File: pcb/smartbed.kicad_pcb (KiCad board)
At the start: 2 copper layers, 59.5 x 51.5 mm, 51 parts, among them J1 USB_MICRO_A, J2 SBBUS_1, J3 DBGCON, J6 FSRCON1, J7 FSRCON2, J8 SBBUS_2, SW1 SW_SPST, U1 LD1117S33CTR, U2 ATSAMD21J18A, Y1 Crystal

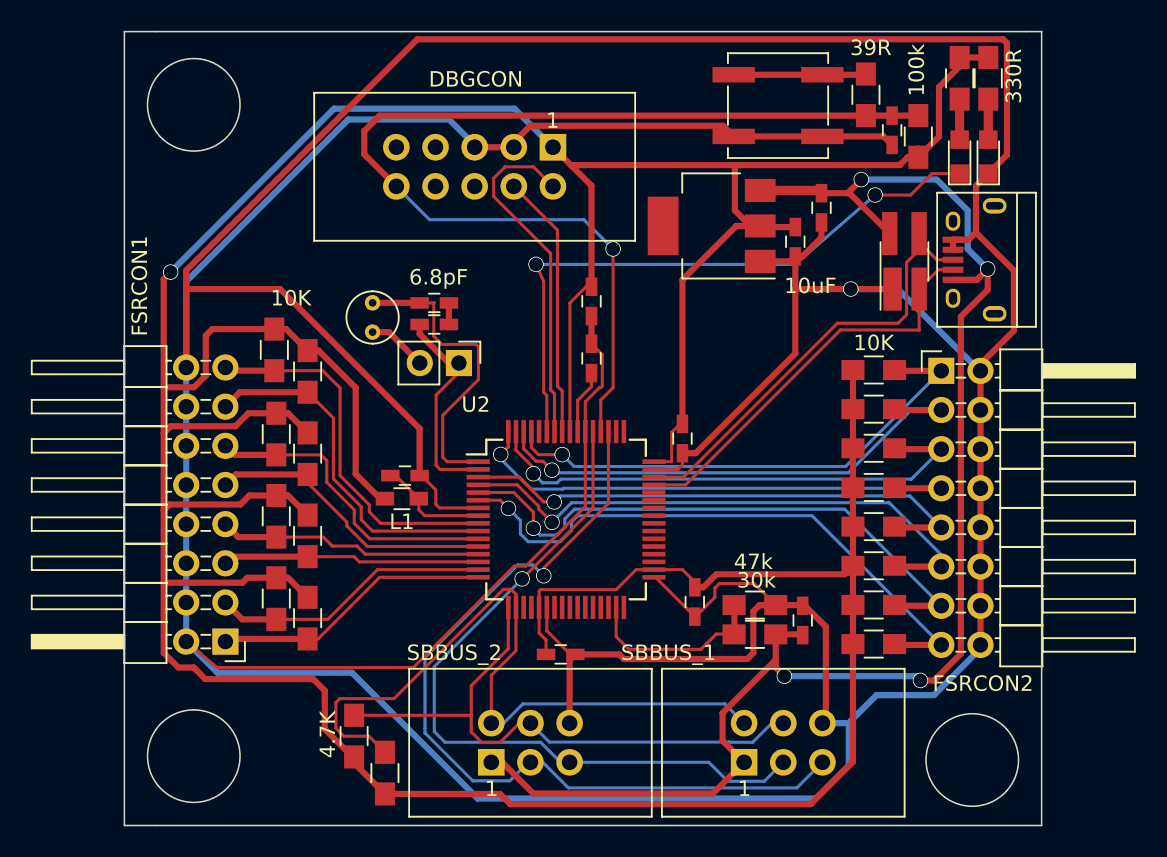
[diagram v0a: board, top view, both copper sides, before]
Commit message: Add ground planes
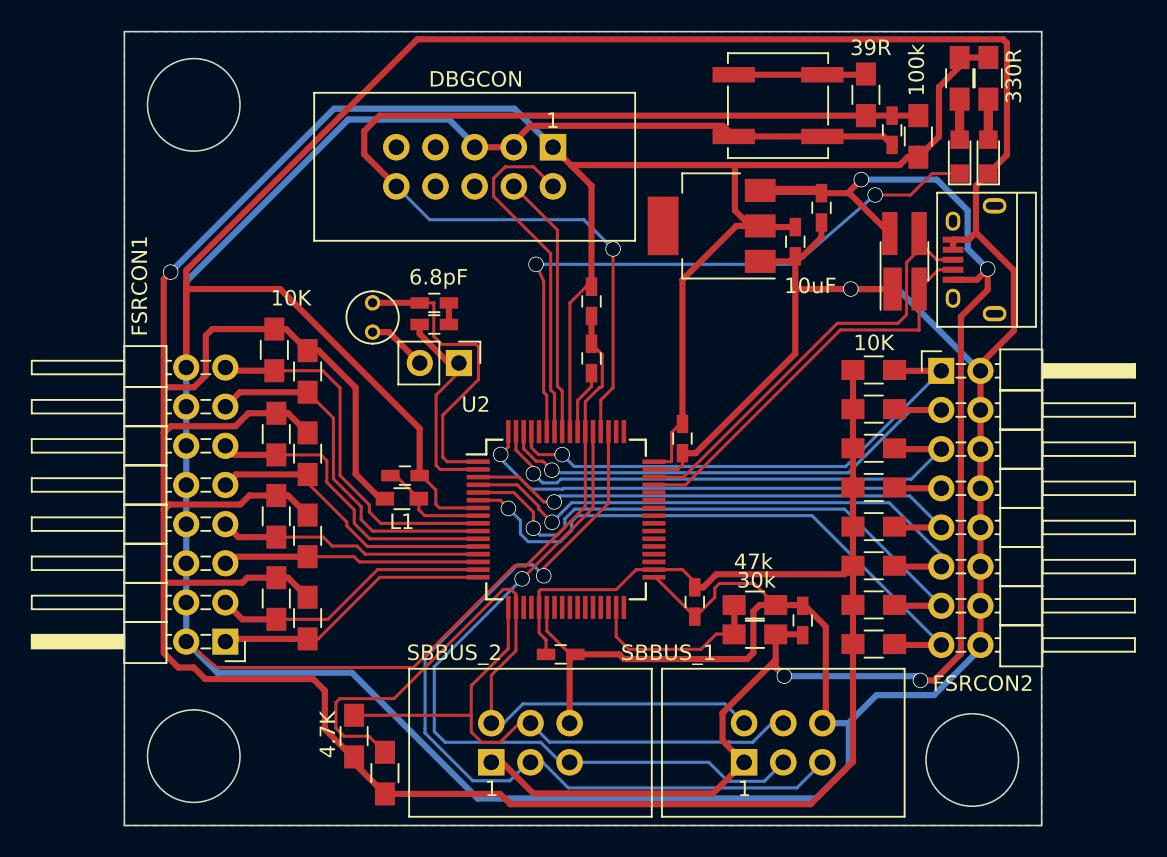
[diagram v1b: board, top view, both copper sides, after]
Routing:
- added copper zone on B.Cu, net GND
- added copper zone on F.Cu, net GND
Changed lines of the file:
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@@
     (mod_text_size 1 1)
     (mod_text_width 0.15)
-    (pad_size 2 3.8)
-    (pad_drill 0)
+    (pad_size 1 1)
+    (pad_drill 0.6)
     (pad_to_mask_clearance 0.2)
     (aux_axis_origin 0 0)
@@
     (fp_circle (center 0.95 0) (end 2.45 0) (layer F.Fab) (width 0.1))
     (fp_circle (center 0.95 0) (end 2.9 0) (layer F.CrtYd) (width 0.05))
-    (pad 1 thru_hole circle (at 0 0 90) (size 1 1) (drill 0.5) (layers *.Cu *.Mask)
+    (pad 1 thru_hole circle (at 0 0 90) (size 1 1) (drill 0.6) (layers *.Cu *.Mask)
       (net 64 "Net-(JP1-Pad2)"))
-    (pad 2 thru_hole circle (at 1.9 0 90) (size 1 1) (drill 0.5) (layers *.Cu *.Mask)
+    (pad 2 thru_hole circle (at 1.9 0 90) (size 1 1) (drill 0.6) (layers *.Cu *.Mask)
       (net 6 XIN))
     (model Crystals.3dshapes/Crystal_Round_d3.0mm_Vertical.wrl
@@
   (segment (start 151.65 63.7) (end 151.65 65.1) (width 0.4) (layer F.Cu) (net 67))
   (segment (start 151.65 65.1) (end 152.1 65.1) (width 0.15) (layer F.Cu) (net 67))
+  (zone (net 1) (net_name GND) (layer F.Cu) (hatch edge 0.508)
+    (connect_pads (clearance 0.508))
+    (min_thickness 0.254)
+    (fill yes (arc_segments 16) (thermal_gap 0.508) (thermal_bridge_width 0.508))
+    (polygon
+      (pts
+        (xy 190.1 97.6) (xy 130.6 97.6) (xy 130.6 46.1) (xy 190.1 46.1)
+      )
+    )
+  )
+  (zone (net 1) (net_name GND) (layer B.Cu) (hatch edge 0.508)
+    (connect_pads (clearance 0.508))
+    (min_thickness 0.254)
+    (fill yes (arc_segments 16) (thermal_gap 0.508) (thermal_bridge_width 0.508))
+    (polygon
+      (pts
+        (xy 190.1 97.6) (xy 130.6 97.6) (xy 130.6 46.1) (xy 190.1 46.1)
+      )
+    )
+  )
 )

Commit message: Updated design to conform HTWG rules
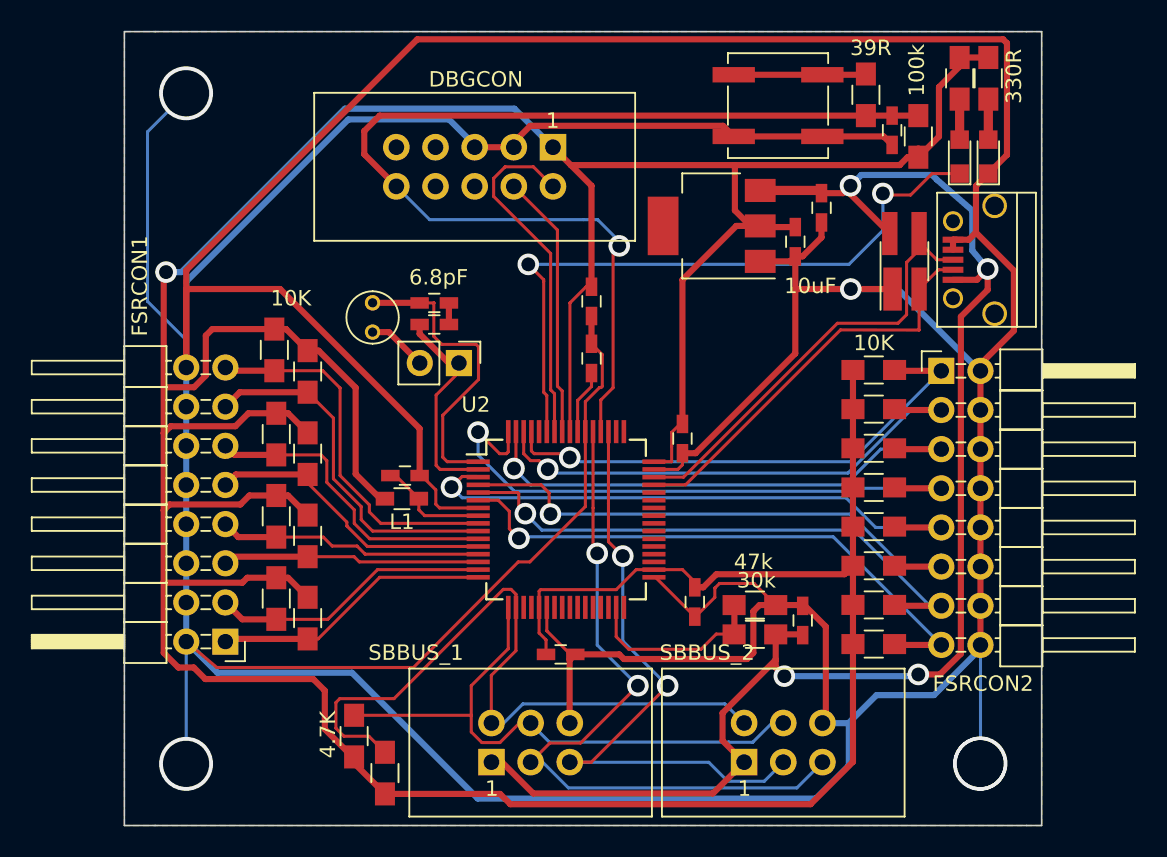
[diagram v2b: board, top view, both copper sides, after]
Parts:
- moved J8 16.4 mm to (170.8, 93.5)
- moved J2 16.4 mm to (154.4, 93.5)
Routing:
- net GND: track 413.2 -> 448.8 mm, vias 1 -> 5
- net SENSE_OUT: track 55.4 -> 41.9 mm, vias 1 -> 2
- net FSR11: track 34.8 -> 39.9 mm
- net FSR12: track 35.2 -> 38.4 mm
- net DBGLED: track 41.0 -> 43.5 mm
- net FSR14: track 38.5 -> 36.6 mm
- net FSR15: track 39.2 -> 37.7 mm
- net SENSE_IN: track 48.2 -> 47.2 mm, vias 1 -> 2
- net RESET: track 68.7 -> 69.6 mm
- net FSR10: track 34.0 -> 34.7 mm
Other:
- outline, holes or cut-outs redrawn
- net class Default: via_dia 1 -> 1.4
